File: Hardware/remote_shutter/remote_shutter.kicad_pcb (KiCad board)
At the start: 4 copper layers, 78 x 57 mm, 66 parts, among them J1 USB_C_Receptacle_USB2.0, J2 OLED, J3 AudioJack3, J4 Buzzer, J5 Conn_01x02_Male, J6 Switch, J7 Conn_01x06_Male, Q1 DMN2056U, Q2 DMN2056U, Q3 BC847BDW1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

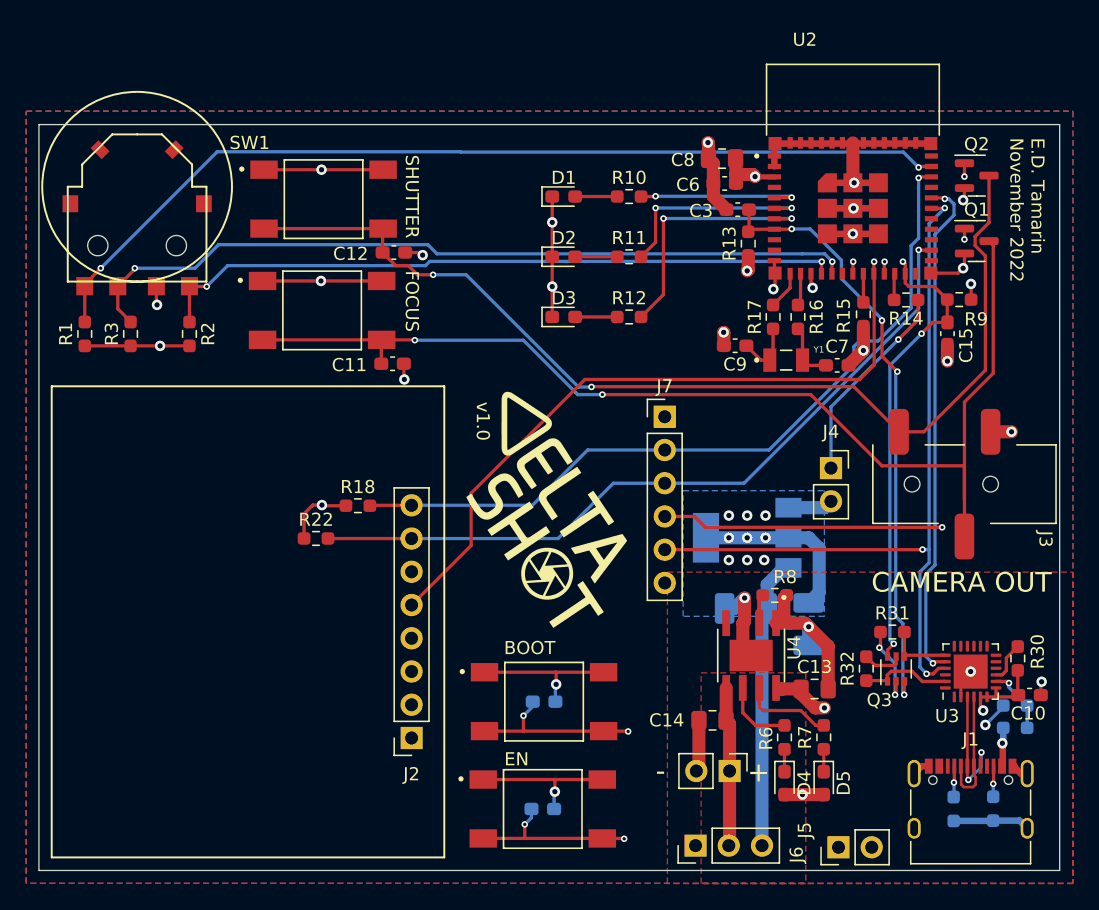
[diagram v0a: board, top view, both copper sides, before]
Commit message: Fixed DRC issues. Updated revision number
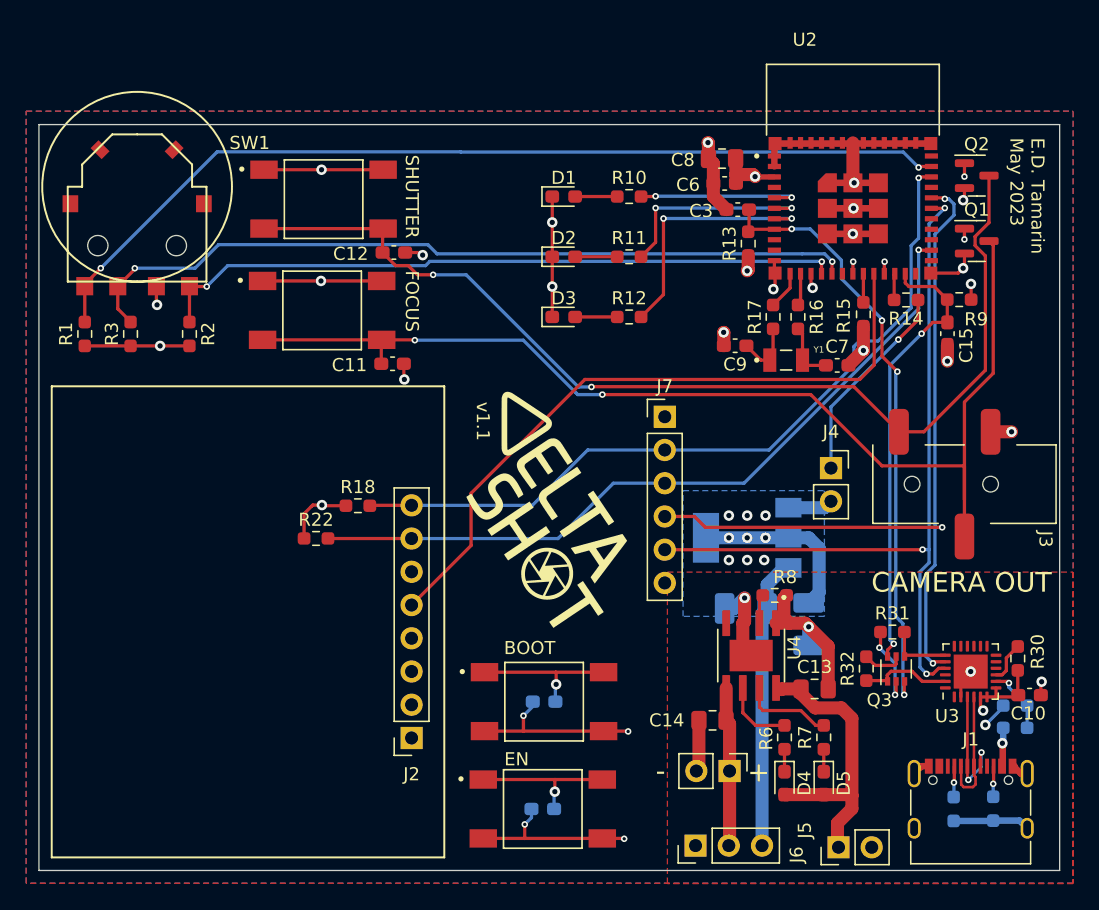
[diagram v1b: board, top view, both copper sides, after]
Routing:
- net /VBUS: track 10.1 -> 25.1 mm, vias 3 -> 1
- net /MCU/IO0: track 72.4 -> 71.4 mm, vias 5 -> 4
- net /MCU/RST: track 53.2 -> 52.3 mm, vias 1 -> 0
- removed copper zone on F.Cu, net /Power/VBAT
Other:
- board text added: "E.D. Tamarin May 2023"
- board text added: "v1.1"
- board text removed: "E.D. Tamarin November 2022"
- board text removed: "v1.0"
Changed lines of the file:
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@@
   )
   (paper "A4")
+  (title_block
+    (title "Remote shutter")
+    (date "2023-05-07")
+    (rev "1.1")
+  )
   (layers
     (0 "F.Cu" signal)
@@
     (effects (font (size 1 1) (thickness 0.15)))
   )
-  (gr_text "E.D. Tamarin\nNovember 2022" (at 179.9775 70.0225 270) (layer "F.SilkS")
+  (gr_text "E.D. Tamarin\nMay 2023" (at 179.9775 70.0225 270) (layer "F.SilkS")
     (effects (font (size 1 1) (thickness 0.15)) (justify left))
   )
@@
     (effects (font (size 1.5 1.5) (thickness 0.3)))
   )
-  (gr_text "v1.0" (at 138.4 91.7 270) (layer "F.SilkS")
+  (gr_text "v1.1" (at 138.4 91.7 270) (layer "F.SilkS")
     (effects (font (size 1 1) (thickness 0.15)))
   )
@@
   (segment (start 173.8875 82.4) (end 173.8875 84.125) (width 0.25) (layer "F.Cu") (net 4))
   (segment (start 141.5275 115.3725) (end 147.6275 115.3725) (width 0.25) (layer "F.Cu") (net 4))
-  (segment (start 170.5 79.5) (end 170.6775 79.6775) (width 0.25) (layer "F.Cu") (net 4))
-  (segment (start 170.6775 79.6775) (end 170.6775 80.4225) (width 0.25) (layer "F.Cu") (net 4))
   (segment (start 172.8875 81.4) (end 173.8875 82.4) (width 0.25) (layer "F.Cu") (net 4))
   (segment (start 147.6275 115.3725) (end 149.4725 115.3725) (width 0.25) (layer "F.Cu") (net 4))
@@
   (via (at 169.8 108.7) (size 0.5) (drill 0.25) (layers "F.Cu" "B.Cu") (net 4))
   (via (at 171.9255 85) (size 0.5) (drill 0.25) (layers "F.Cu" "B.Cu") (net 4))
-  (via (at 170.5 79.5) (size 0.5) (drill 0.25) (layers "F.Cu" "B.Cu") (net 4))
   (via (at 141.5 114.2) (size 0.5) (drill 0.25) (layers "F.Cu" "B.Cu") (net 4))
   (via (at 149.5 115.4) (size 0.5) (drill 0.25) (layers "F.Cu" "B.Cu") (net 4))
@@
   (segment (start 137.5 101.19) (end 132.9525 105.7375) (width 0.25) (layer "F.Cu") (net 11))
   (segment (start 168.2775 80.4225) (end 168.30202 80.44702) (width 0.25) (layer "F.Cu") (net 11))
-  (segment (start 168.2775 79.5225) (end 168.3 79.5) (width 0.25) (layer "F.Cu") (net 11))
-  (segment (start 168.2775 80.4225) (end 168.2775 79.5225) (width 0.25) (layer "F.Cu") (net 11))
   (segment (start 167.2 88.5) (end 146.2 88.5) (width 0.25) (layer "F.Cu") (net 11))
   (segment (start 168.30202 87.39798) (end 167.2 88.5) (width 0.25) (layer "F.Cu") (net 11))
   (segment (start 137.5 97.2) (end 137.5 101.19) (width 0.25) (layer "F.Cu") (net 11))
   (segment (start 168.30202 80.44702) (end 168.30202 87.39798) (width 0.25) (layer "F.Cu") (net 11))
-  (via (at 168.3 79.5) (size 0.5) (drill 0.25) (layers "F.Cu" "B.Cu") (net 11))
   (segment (start 171.6525 83.94708) (end 171.6525 82.4225) (width 0.25) (layer "F.Cu") (net 14))
   (segment (start 170.14979 85.44979) (end 171.6525 83.94708) (width 0.25) (layer "F.Cu") (net 14))
@@
   (segment (start 169.9775 110.2475) (end 169.87452 110.35048) (width 0.25) (layer "F.Cu") (net 22))
   (segment (start 168.36298 110.35048) (end 167.7 109.6875) (width 0.25) (layer "F.Cu") (net 22))
-  (segment (start 167.7 109.6875) (end 167.7 109.7) (width 0.25) (layer "F.Cu") (net 22))
   (segment (start 169.87452 110.35048) (end 168.36298 110.35048) (width 0.25) (layer "F.Cu") (net 22))
   (segment (start 169.9775 109.6725) (end 169.9775 110.2475) (width 0.25) (layer "F.Cu") (net 22))
@@
   (segment (start 179.2775 110.735) (end 179.2775 112.585) (width 0.25) (layer "F.Cu") (net 56))
   (segment (start 175.7125 81.2125) (end 175.7 81.2) (width 0.25) (layer "F.Cu") (net 56))
-  (segment (start 178.94 111.0725) (end 179.2775 110.735) (width 0.25) (layer "F.Cu") (net 56))
   (segment (start 177.615 112.685) (end 177.54 112.76) (width 0.25) (layer "F.Cu") (net 56))
   (segment (start 124.7375 98.7625) (end 125.3 98.2) (width 0.25) (layer "F.Cu") (net 56))
@@
   (segment (start 163.3 100.6) (end 164.1 101.4) (width 1) (layer "B.Cu") (net 56))
   (segment (start 161.75 100.6) (end 163.3 100.6) (width 1) (layer "B.Cu") (net 56))
+  (segment (start 165.5 122.4) (end 165.5 124.175) (width 1) (layer "F.Cu") (net 57))
   (segment (start 178.1 116.3) (end 178.127989 116.327989) (width 0.5) (layer "F.Cu") (net 57))
-  (segment (start 162.7125 112.15) (end 162.7125 112.5125) (width 1) (layer "F.Cu") (net 57))
+  (segment (start 165.8 113.6) (end 166.6 114.4) (width 1) (layer "F.Cu") (net 57))
+  (segment (start 166.6 120.3) (end 166.6 121.3) (width 1) (layer "F.Cu") (net 57))
   (segment (start 161.45 120.225) (end 164.45 120.225) (width 1) (layer "F.Cu") (net 57))
-  (segment (start 163.8 113.6) (end 164.5 113.6) (width 1) (layer "F.Cu") (net 57))
-  (segment (start 162.7125 112.5125) (end 163.8 113.6) (width 1) (layer "F.Cu") (net 57))
+  (segment (start 166.525 120.225) (end 166.6 120.3) (width 1) (layer "F.Cu") (net 57))
+  (segment (start 162.7125 112.15) (end 162.7125 112.5125) (width 1) (layer "F.Cu") (net 57))
+  (segment (start 163.8 113.6) (end 165.8 113.6) (width 1) (layer "F.Cu") (net 57))
+  (segment (start 166.6 121.3) (end 165.5 122.4) (width 1) (layer "F.Cu") (net 57))
+  (segment (start 165.5 124.175) (end 165.575 124.25) (width 1) (layer "F.Cu") (net 57))
   (segment (start 178.127989 116.327989) (end 178.127989 118.0525) (width 0.5) (layer "F.Cu") (net 57))
   (segment (start 162.7125 112.15) (end 161.25 112.15) (width 1) (layer "F.Cu") (net 57))
   (segment (start 161.25 112.15) (end 161.2 112.2) (width 1) (layer "F.Cu") (net 57))
+  (segment (start 162.7125 112.5125) (end 163.8 113.6) (width 1) (layer "F.Cu") (net 57))
+  (segment (start 166.6 114.4) (end 166.6 120.3) (width 1) (layer "F.Cu") (net 57))
+  (segment (start 164.45 120.225) (end 166.525 120.225) (width 1) (layer "F.Cu") (net 57))
   (via (at 178.1 116.3) (size 0.8) (drill 0.4) (layers "F.Cu" "B.Cu") (net 57))
-  (via (at 164.5 113.6) (size 0.8) (drill 0.4) (layers "F.Cu" "B.Cu") (net 57))
-  (via (at 162.825 120.225) (size 0.8) (drill 0.4) (layers "F.Cu" "B.Cu") (net 57))
   (segment (start 178.165 116.235) (end 178.1 116.3) (width 0.5) (layer "B.Cu") (net 57))
   (segment (start 178.165 115.1225) (end 178.165 116.235) (width 0.5) (layer "B.Cu") (net 57))
@@
   (segment (start 132.9525 100.6575) (end 144.1425 100.6575) (width 0.25) (layer "B.Cu") (net 76))
   (segment (start 171.7 78.6) (end 171.7 83.087114) (width 0.25) (layer "B.Cu") (net 76))
-  (zone (net 58) (net_name "/Power/VBAT") (layer "F.Cu") (hatch edge 0.508)
-    (priority 1)
-    (connect_pads (clearance 0.254))
-    (min_thickness 0.254) (filled_areas_thickness no)
-    (fill yes (thermal_gap 0.254) (thermal_bridge_width 0.508))
-    (polygon
-      (pts
-        (xy 163.0775 127.0225)
-        (xy 155.0775 127.0225)
-        (xy 155.0775 110.9225)
-        (xy 163.0775 110.9225)
-      )
-    )
-  )
   (zone (net 0) (net_name "") (layer "F.Cu") (hatch edge 0.508)
     (connect_pads (clearance 0.254))
